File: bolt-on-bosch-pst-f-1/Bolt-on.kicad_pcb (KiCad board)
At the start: 2 copper layers, 42 x 72 mm, 14 parts

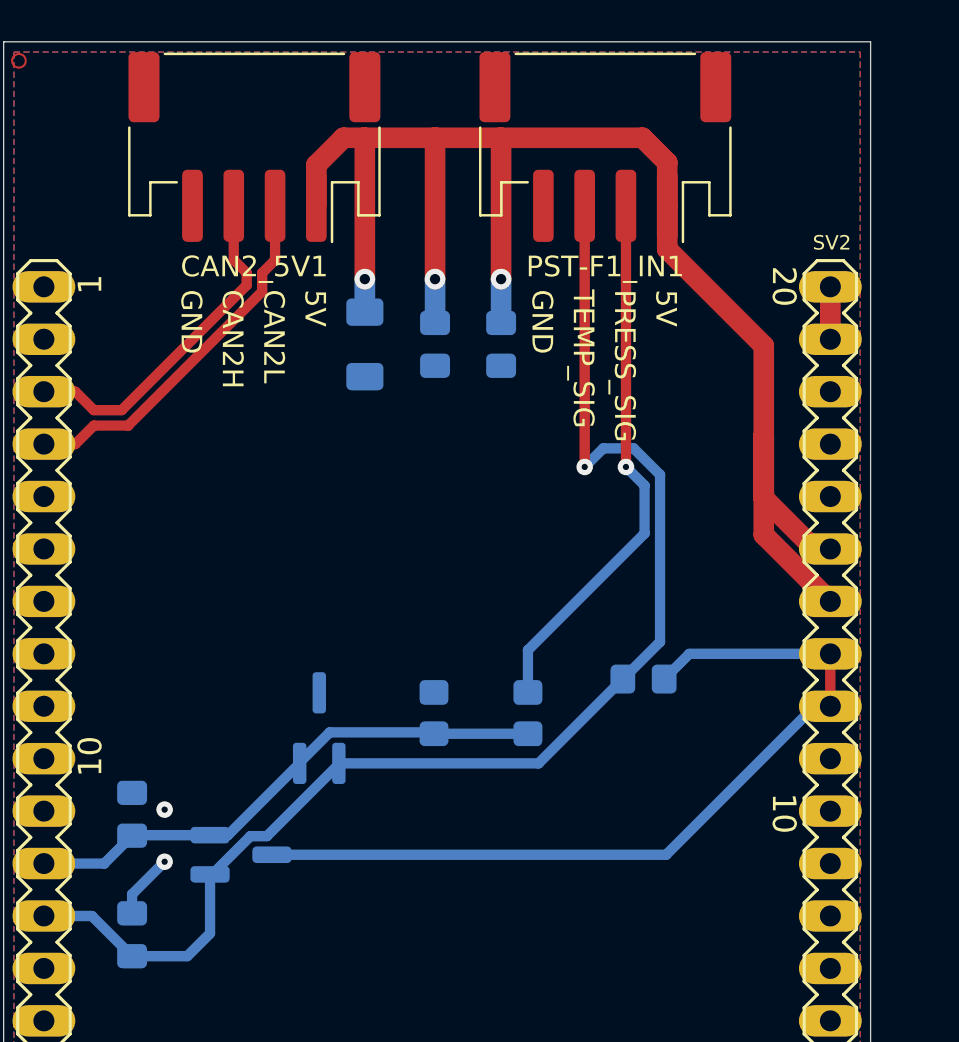
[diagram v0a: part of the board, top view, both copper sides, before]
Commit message: pcb added tented gnd vias
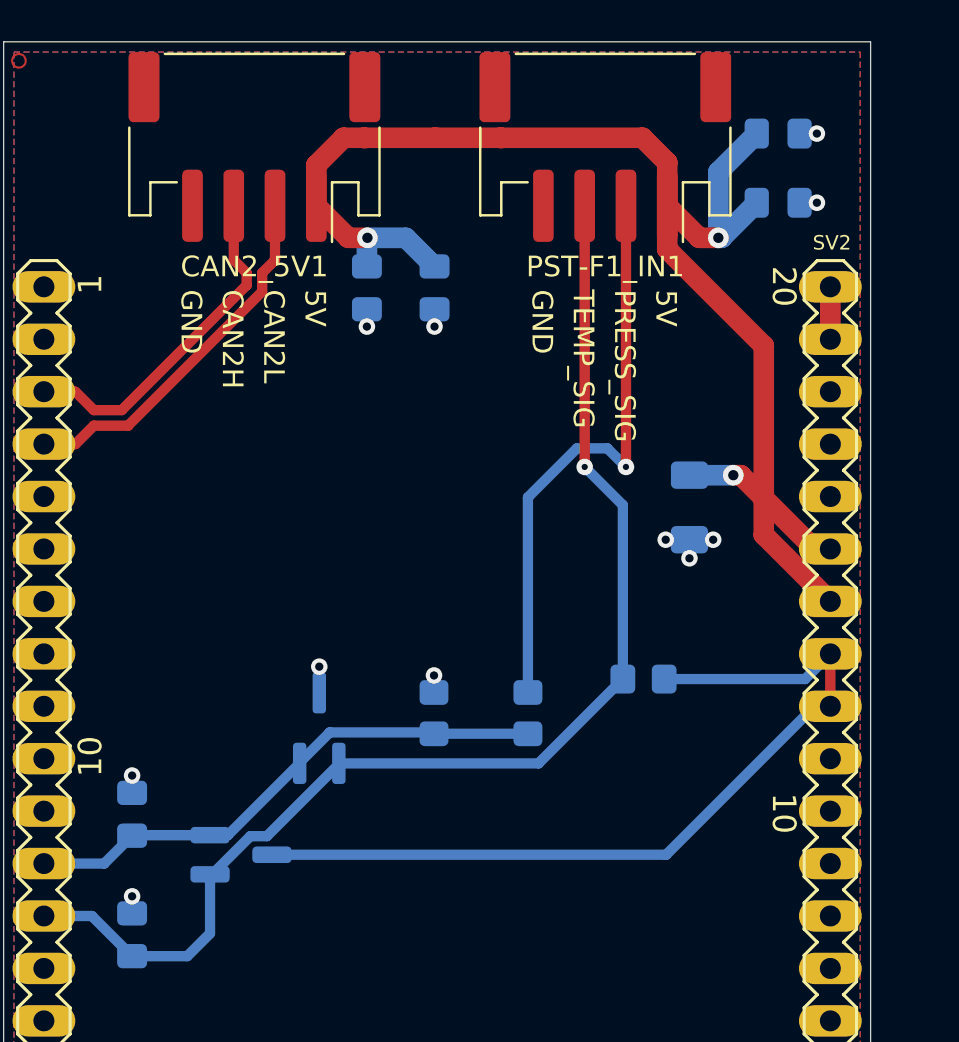
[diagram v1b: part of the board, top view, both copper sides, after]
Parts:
- added C3: ﻿0.1µF, Capacitor_SMD:C_0805_2012Metric_Pad1.18x1.45mm_HandSolder, B.Cu at (165.0, 76.8)
- added C5: 1µF, Capacitor_SMD:C_0805_2012Metric_Pad1.18x1.45mm_HandSolder, B.Cu at (165.0, 73.5)
- moved C7 17.6 mm to (160.7, 91.6)
- moved C4 7.05 mm to (145.1, 80.9)
- moved C6 2.74 mm to (148.4, 80.9)
- renumbered C3 to C4, C4 to C6, C5 to C7
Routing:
- net /+5V: track 78.2 -> 72.8 mm
- net /IO36: track 64.3 -> 59.8 mm
- net GND: track 3.15 -> 0.00 mm, vias 2 -> 11
- net Net-(PST-F1_IN1-PRESS_SIG): track 26.3 -> 28.2 mm
